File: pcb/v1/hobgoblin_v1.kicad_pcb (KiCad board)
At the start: 2 copper layers, 160 x 115 mm, 55 parts, among them J1 5V, J2 RC2014EXT1, J3 RC2014EXT2, J4 USB_B_Mini, SW1 RESET, SW2 ROMBNK, U1 74LS32, U10 FT232RL, U2 Z80CPU, U3 74LS14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

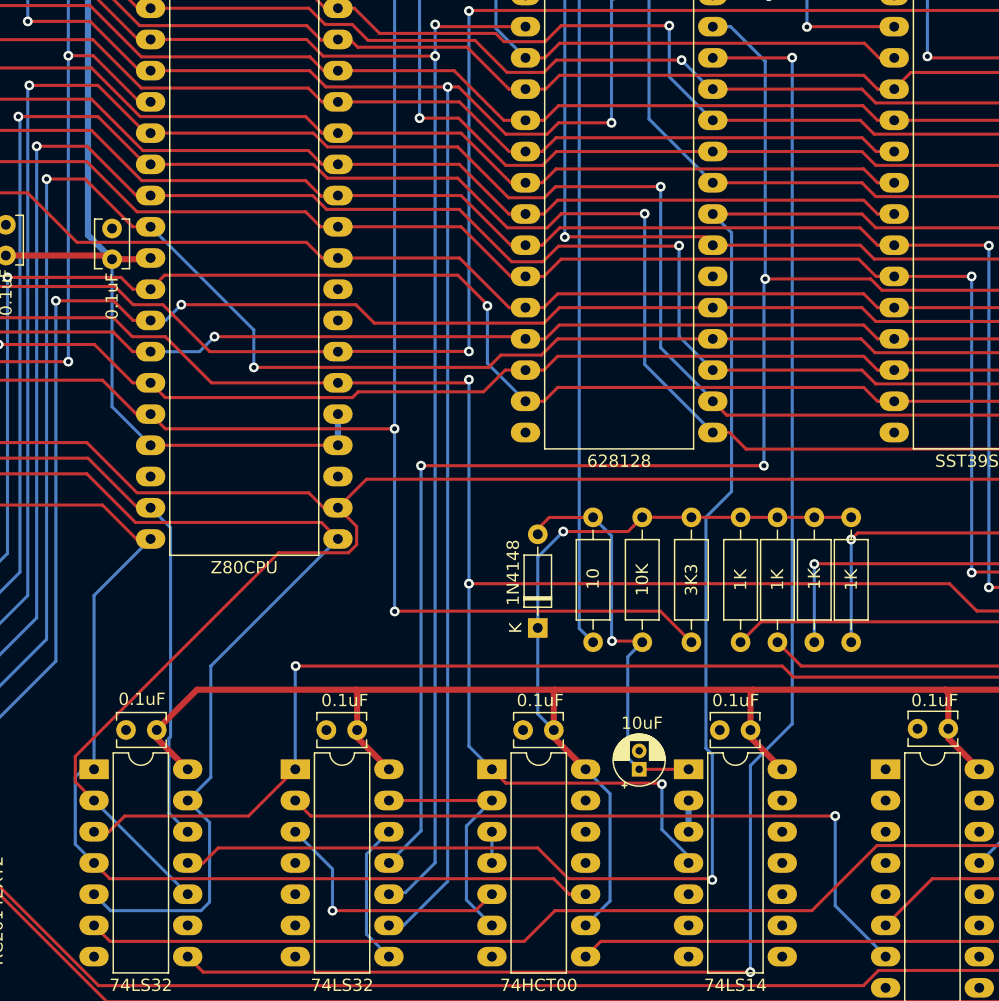
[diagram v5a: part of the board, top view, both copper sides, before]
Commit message: Add missing traces
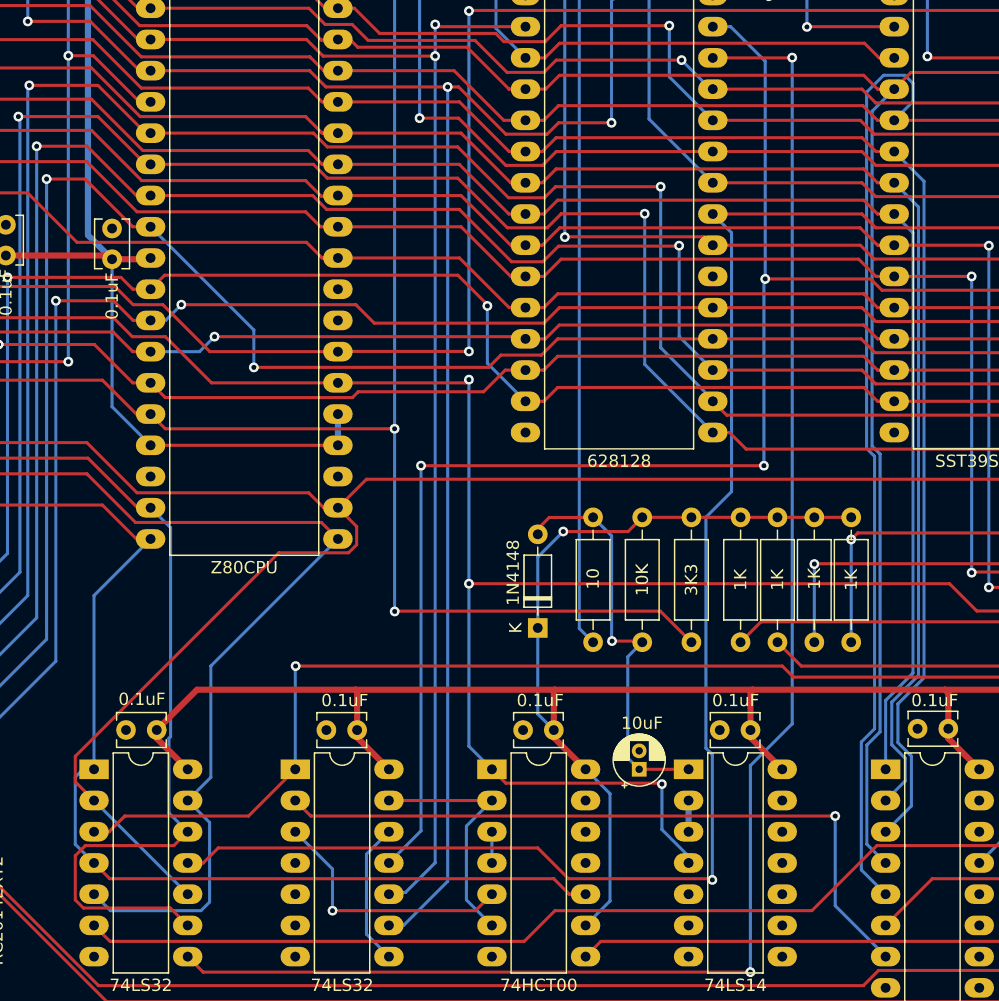
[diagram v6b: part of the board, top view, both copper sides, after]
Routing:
- net /A6: track 139.4 -> 214.5 mm
- net /A7: track 139.4 -> 204.5 mm
- net /A5: track 95.3 -> 153.9 mm
- net /A4: track 95.3 -> 148.4 mm
- net /A3: track 95.3 -> 142.0 mm
- net /~MREQ: track 79.8 -> 103.4 mm

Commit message: Final 1.3 routing improvements
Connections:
- U4 pad 6: VCC -> /~M1
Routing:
- net /~M1: track 174.5 -> 250.1 mm
- net VCC: track 645.8 -> 629.5 mm
- net /~MREQ: track 103.4 -> 88.7 mm
- net /ROMBNK1: track 53.0 -> 48.8 mm, vias 1 -> 0
- net /~RD: track 93.0 -> 96.3 mm
- net /~IORD: track 103.0 -> 106.1 mm
- net /D6: track 230.1 -> 228.2 mm
- net /~PORT38: track 57.6 -> 56.7 mm
- net /~INT: track 221.1 -> 220.1 mm
- net /~RESET: track 171.7 -> 171.2 mm
